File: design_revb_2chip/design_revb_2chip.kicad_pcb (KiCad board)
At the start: 4 copper layers, 0 parts

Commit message: PCB Created
Footprints all placed in the PCB document
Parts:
- added C1: 0.1uF, Capacitor_SMD:C_0201_0603Metric, F.Cu at (72.2, 53.8)
- added C10: 0.1uF, Capacitor_SMD:C_0201_0603Metric, F.Cu at (74.6, 57.2)
- added C11: 0.1uF, Capacitor_SMD:C_0201_0603Metric, F.Cu at (74.6, 59.0)
- added C12: 0.1uF, Capacitor_SMD:C_0201_0603Metric, F.Cu at (74.6, 60.8)
- added C13: 22uF, Capacitor_SMD:C_0201_0603Metric, F.Cu at (74.6, 62.5)
- added C14: 0.1uF, Capacitor_SMD:C_0201_0603Metric, F.Cu at (74.6, 64.2)
- added C15: 0.1uF, Capacitor_SMD:C_0201_0603Metric, F.Cu at (77.1, 53.8)
- added C16: 10uF, Capacitor_SMD:C_0201_0603Metric, F.Cu at (77.1, 55.5)
- added C17: 0.1uF, Capacitor_SMD:C_0201_0603Metric, F.Cu at (77.1, 57.2)
- added C18: 4.7uF, Capacitor_SMD:C_0201_0603Metric, F.Cu at (77.1, 59.0)
- added C19: 0.1uF, Capacitor_SMD:C_0201_0603Metric, F.Cu at (77.1, 60.8)
- added C2: 0.1uF, Capacitor_SMD:C_0201_0603Metric, F.Cu at (72.2, 55.5)
- added C20: 1uF, Capacitor_SMD:C_0201_0603Metric, F.Cu at (77.1, 62.5)
- added C21: 22uF, Capacitor_SMD:C_0201_0603Metric, F.Cu at (77.1, 64.2)
- added C22: 0.1uF, Capacitor_SMD:C_0201_0603Metric, F.Cu at (79.5, 53.8)
- added C23: 0.1uF, Capacitor_SMD:C_0201_0603Metric, F.Cu at (79.5, 55.5)
- added C24: 16pf, Capacitor_SMD:C_0201_0603Metric, F.Cu at (79.5, 57.2)
- added C25: 0.1uF, Capacitor_SMD:C_0201_0603Metric, F.Cu at (79.5, 59.0)
- added C26: 16pf, Capacitor_SMD:C_0201_0603Metric, F.Cu at (79.5, 60.8)
- added C27: 0.1uF, Capacitor_SMD:C_0201_0603Metric, F.Cu at (91.3, 86.5)
- added C28: 0.1uF, Capacitor_SMD:C_0201_0603Metric, F.Cu at (91.3, 88.2)
- added C29: 4.7nF, Capacitor_SMD:C_0201_0603Metric, F.Cu at (91.3, 90.0)
- added C3: 1uF, Capacitor_SMD:C_0201_0603Metric, F.Cu at (72.2, 57.2)
- added C30: 1uF, Capacitor_SMD:C_0201_0603Metric, F.Cu at (91.3, 91.8)
- added C31: 1uF, Capacitor_SMD:C_0201_0603Metric, F.Cu at (91.3, 93.5)
- added C32: 1uF, Capacitor_SMD:C_0201_0603Metric, F.Cu at (91.3, 95.2)
- added C33: 10uF, Capacitor_SMD:C_0201_0603Metric, F.Cu at (93.8, 86.5)
- added C34: 1uF, Capacitor_SMD:C_0201_0603Metric, F.Cu at (93.8, 88.2)
- added C35: 2.2uF, Capacitor_SMD:C_0201_0603Metric, F.Cu at (93.8, 90.0)
- added C36: 100nF, Capacitor_SMD:C_0201_0603Metric, F.Cu at (93.8, 91.8)
- added C37: 2.2uF, Capacitor_SMD:C_0201_0603Metric, F.Cu at (93.8, 93.5)
- added C38: 2.2uF, Capacitor_SMD:C_0201_0603Metric, F.Cu at (93.8, 95.2)
- added C39: 2.2uF, Capacitor_SMD:C_0201_0603Metric, F.Cu at (96.2, 86.5)
- added C4: 0.1uF, Capacitor_SMD:C_0201_0603Metric, F.Cu at (72.2, 59.0)
- added C40: 100nF, Capacitor_SMD:C_0201_0603Metric, F.Cu at (96.2, 88.2)
- added C41: 100nF, Capacitor_SMD:C_0201_0603Metric, F.Cu at (96.2, 90.0)
- added C42: 100nF, Capacitor_SMD:C_0201_0603Metric, F.Cu at (96.2, 91.8)
- added C43: 100nF, Capacitor_SMD:C_0201_0603Metric, F.Cu at (96.2, 93.5)
- added C44: 10nF, Capacitor_SMD:C_0201_0603Metric, F.Cu at (96.2, 95.2)
- added C45: 10nF, Capacitor_SMD:C_0201_0603Metric, F.Cu at (98.7, 86.5)
- added C46: 10nF, Capacitor_SMD:C_0201_0603Metric, F.Cu at (98.7, 88.2)
- added C47: 10nF, Capacitor_SMD:C_0201_0603Metric, F.Cu at (98.7, 90.0)
- added C48: 10nF, Capacitor_SMD:C_0201_0603Metric, F.Cu at (98.7, 91.8)
- added C49: 10uF, Capacitor_SMD:C_0201_0603Metric, F.Cu at (98.7, 93.5)
- added C5: 0.1uF, Capacitor_SMD:C_0201_0603Metric, F.Cu at (72.2, 60.8)
- added C6: 1uF, Capacitor_SMD:C_0201_0603Metric, F.Cu at (72.2, 62.5)
- added C7: 0.1uF, Capacitor_SMD:C_0201_0603Metric, F.Cu at (72.2, 64.2)
- added C8: 0.1uF, Capacitor_SMD:C_0201_0603Metric, F.Cu at (74.6, 53.8)
- added C9: 0.1uF, Capacitor_SMD:C_0201_0603Metric, F.Cu at (74.6, 55.5)
- added D1: GREEN, LED_SMD:LED_0603_1608Metric, F.Cu at (95.7, 62.5)
- added D2: GREEN, LED_SMD:LED_0603_1608Metric, F.Cu at (95.7, 65.1)
- added D3: LED, LED_SMD:LED_0603_1608Metric, F.Cu at (81.5, 90.9)
- added D4: LED, LED_SMD:LED_0603_1608Metric, F.Cu at (81.5, 93.5)
- added D5: LED, LED_SMD:LED_0603_1608Metric, F.Cu at (81.5, 96.0)
- added FB1: FerriteBead, Capstone_Footprints:BEADC1608X95N, F.Cu at (99.7, 62.4)
- added FB2: FerriteBead, Capstone_Footprints:BEADC1608X95N, F.Cu at (99.7, 65.0)
- added J1: USB_C_Receptacle, Connector_USB:USB_C_Receptacle_Amphenol_12401610E4-2A_CircularHoles, F.Cu at (159.3, 72.5)
- added J2: Conn_01x08, Connector_PinHeader_2.00mm:PinHeader_1x08_P2.00mm_Horizontal, F.Cu at (170.0, 93.0)
- added J3: 09452812810, Capstone_Footprints:09452812810, F.Cu at (246.3, 72.2)
- added JP1: Jumper_2_Bridged, Jumper:SolderJumper-2_P1.3mm_Bridged_Pad1.0x1.5mm, F.Cu at (99.8, 72.7)
- added JP2: Jumper_2_Open, Jumper:SolderJumper-3_P1.3mm_Open_Pad1.0x1.5mm, F.Cu at (87.3, 87.4)
- added JP3: Jumper_2_Open, Jumper:SolderJumper-3_P1.3mm_Open_Pad1.0x1.5mm, F.Cu at (87.3, 91.2)
- added JP4: Jumper_2_Open, Jumper:SolderJumper-3_P1.3mm_Open_Pad1.0x1.5mm, F.Cu at (87.3, 95.1)
- added JP5: Jumper_2_Bridged, Jumper:SolderJumper-2_P1.3mm_Bridged_Pad1.0x1.5mm, F.Cu at (99.8, 76.2)
- added L1: 3.3uH, Inductor_SMD_Wurth:L_Wurth_WE-LQSH-3012, F.Cu at (88.2, 64.5)
- added L2: 2.2uH, Inductor_SMD:L_1008_2520Metric, F.Cu at (67.9, 81.0)
- added R1: 1k, Resistor_SMD:R_0805_2012Metric, F.Cu at (83.4, 36.3)
- added R10: 10k, Resistor_SMD:R_0805_2012Metric, F.Cu at (87.8, 42.2)
- added R11: 470k, Resistor_SMD:R_0805_2012Metric, F.Cu at (87.8, 45.1)
- added R12: 150k, Resistor_SMD:R_0805_2012Metric, F.Cu at (87.8, 48.1)
- added R13: 10k, Resistor_SMD:R_0805_2012Metric, F.Cu at (92.2, 36.3)
- added R14: 10k, Resistor_SMD:R_0805_2012Metric, F.Cu at (92.2, 39.2)
- added R15: 330R, Resistor_SMD:R_0805_2012Metric, F.Cu at (92.2, 42.2)
- added R16: 10k, Resistor_SMD:R_0805_2012Metric, F.Cu at (86.6, 72.3)
- added R17: 1k, Resistor_SMD:R_0805_2012Metric, F.Cu at (86.6, 75.3)
- added R18: 1k, Resistor_SMD:R_0805_2012Metric, F.Cu at (86.6, 78.2)
- added R19: 100k, Resistor_SMD:R_0805_2012Metric, F.Cu at (86.6, 81.2)
- added R2: 10k, Resistor_SMD:R_0805_2012Metric, F.Cu at (83.4, 39.2)
- added R20: 2.2k, Resistor_SMD:R_0805_2012Metric, F.Cu at (86.6, 84.2)
- added R21: 2.49k, Resistor_SMD:R_0805_2012Metric, F.Cu at (91.0, 72.3)
- added R22: 470, Resistor_SMD:R_0805_2012Metric, F.Cu at (91.0, 75.3)
- added R23: 470, Resistor_SMD:R_0805_2012Metric, F.Cu at (91.0, 78.2)
- added R24: 2.49k, Resistor_SMD:R_0805_2012Metric, F.Cu at (91.0, 81.2)
- added R25: 470, Resistor_SMD:R_0805_2012Metric, F.Cu at (91.0, 84.2)
- added R26: 2.49k, Resistor_SMD:R_0805_2012Metric, F.Cu at (95.5, 72.3)
- added R27: 2.49k, Resistor_SMD:R_0805_2012Metric, F.Cu at (95.5, 75.3)
- added R28: 2.49k, Resistor_SMD:R_0805_2012Metric, F.Cu at (95.5, 78.2)
- added R29: 2.49k, Resistor_SMD:R_0805_2012Metric, F.Cu at (95.5, 81.2)
- added R3: 10k, Resistor_SMD:R_0805_2012Metric, F.Cu at (83.4, 42.2)
- added R4: 1k, Resistor_SMD:R_0805_2012Metric, F.Cu at (83.4, 45.1)
- added R5: 10k, Resistor_SMD:R_0805_2012Metric, F.Cu at (83.4, 48.1)
- added R6: 12k, Resistor_SMD:R_0402_1005Metric, F.Cu at (103.1, 62.2)
- added R7: 10k, Resistor_SMD:R_0805_2012Metric, F.Cu at (87.8, 36.3)
- added R8: 2k, Resistor_SMD:R_0402_1005Metric, F.Cu at (103.1, 64.2)
- added R9: 100k, Resistor_SMD:R_0805_2012Metric, F.Cu at (87.8, 39.2)
- added U1: LAN7801-I/9JX, Capstone_Footprints:SQFN64_9JX_MCH, F.Cu at (189.8, 73.6)
- added U2: TPS62162QDSGRQ1, Capstone_Footprints:DSG0008A, F.Cu at (192.5, 88.3)
- added U3: 93C56A-I/P, Capstone_Footprints:PDIP8_300MC_MCH, F.Cu at (175.9, 54.4)
- added U4: DP83TG720SWRHARQ1, Capstone_Footprints:VQFN36_6X6_TEX, F.Cu at (216.0, 73.6)
- added U5: TPS784105QWDRBRQ1, Capstone_Footprints:DRB0008J-IPC_A, F.Cu at (241.0, 69.5)
- added XTAL1: ECS-250-18-36B2-CTY-TR, Capstone_Footprints:ECX-2236B2_ECS, F.Cu at (179.0, 94.9)

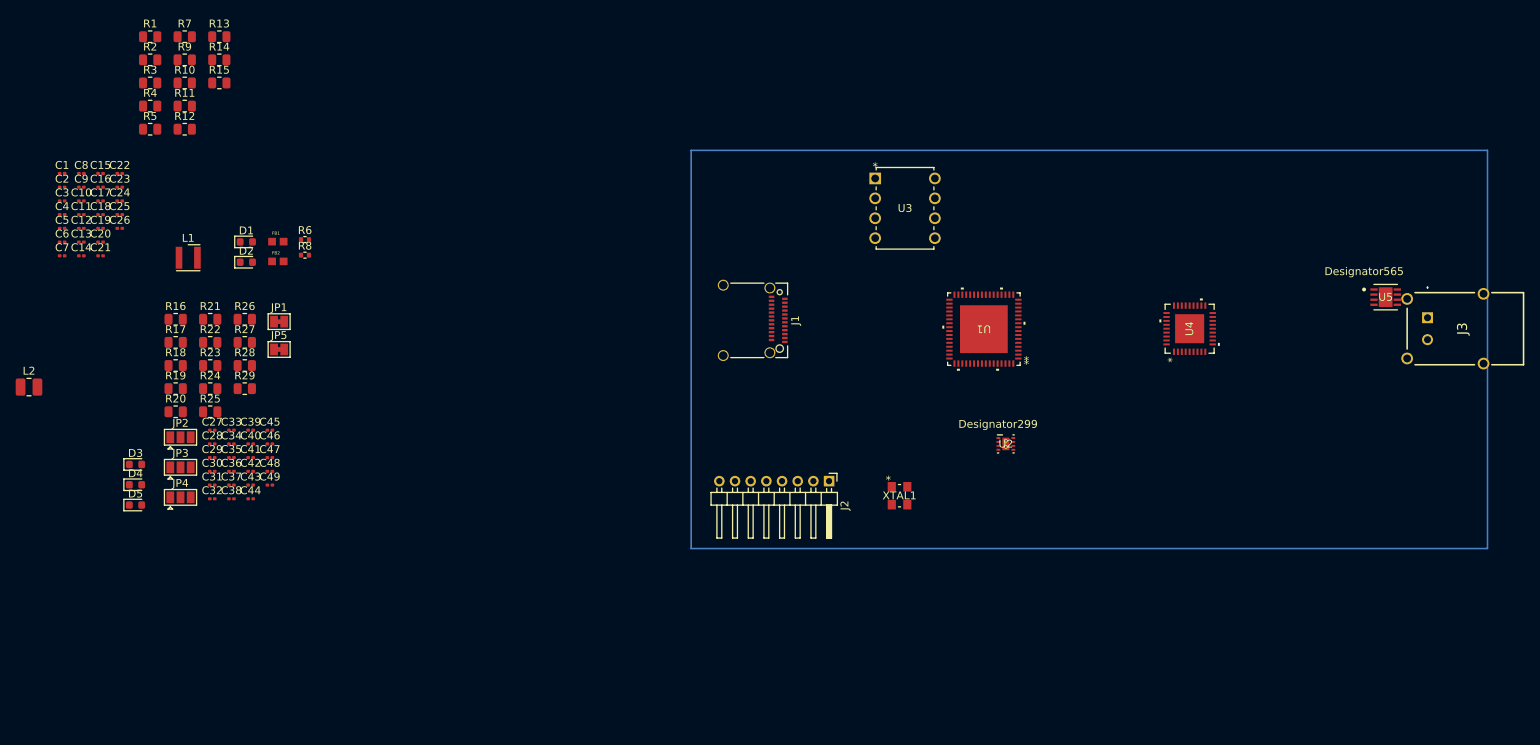
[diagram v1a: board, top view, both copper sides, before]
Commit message: Some PCB Design
- USB side PCB design (mostly done)
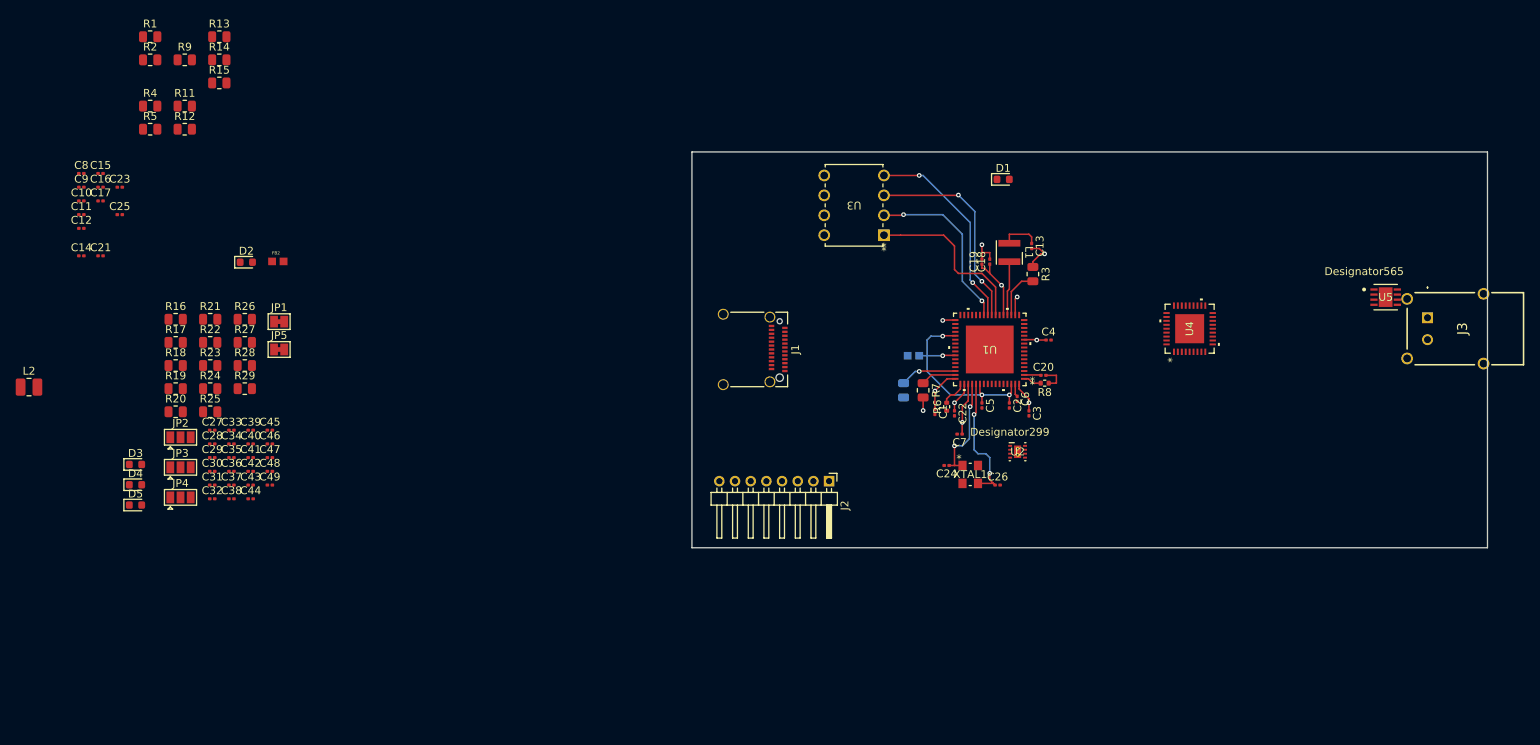
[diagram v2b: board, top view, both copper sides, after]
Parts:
- FB1, R10: moved to B.Cu
- moved C4 126.9 mm to (198.0, 75.0)
- moved C3 126.3 mm to (195.5, 84.3), turned to -90 degrees
- moved C2 124.0 mm to (193.0, 83.3), turned to -90 degrees
- moved C6 123.5 mm to (194.0, 82.5), turned to -90 degrees
- moved C20 121.5 mm to (197.3, 79.5)
- moved C13 121.2 mm to (195.8, 63.0), turned to -90 degrees
- moved C5 119.5 mm to (189.5, 83.3), turned to -90 degrees
- moved C7 116.7 mm to (186.7, 87.0), turned to 180 degrees
- moved C26 116.7 mm to (191.5, 93.5)
- moved C1 115.4 mm to (183.5, 84.2), turned to -90 degrees
- moved R3 115.2 mm to (196.0, 66.6), turned to -90 degrees
- moved C18 113.6 mm to (190.5, 65.0), turned to 90 degrees
- moved C19 112.5 mm to (189.5, 65.0), turned to 90 degrees
- moved C22 110.8 mm to (186.0, 84.3), turned to -90 degrees
- moved C24 110.8 mm to (185.0, 91.0), turned to 180 degrees
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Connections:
- C23 pad 1: VPP -> VDD33A
- U1 pad 33: VPP -> VDD33A
- U3 pad 8: VPP -> VDD33A
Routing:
- net VDD33A: track 0.00 -> 63.6 mm, vias 0 -> 9
- net VDD12A: track 0.00 -> 29.3 mm, vias 0 -> 4
- net Net-(U1-EEDI/GPIO1): track 0.00 -> 26.6 mm, vias 0 -> 2
- net Net-(U1-EEDO/GPIO2): track 0.00 -> 26.2 mm, vias 0 -> 2
- net Net-(U1-EECLK/GPIO3): track 0.00 -> 22.5 mm, vias 0 -> 2
- net Net-(U1-EECS/GPIO0): track 0.00 -> 22.3 mm
- net XO: track 0.00 -> 17.0 mm, vias 0 -> 2
- net GND: track 0.00 -> 13.9 mm, vias 0 -> 2
- net XI: track 0.00 -> 13.6 mm, vias 0 -> 2
- net TEST: track 0.00 -> 7.25 mm, vias 0 -> 1
- net VDD12_SW_OUT: track 0.00 -> 6.91 mm
- net Net-(U1-CLK125): track 0.00 -> 6.29 mm
- net VDD12: track 0.00 -> 4.97 mm
- net RESET_N: track 0.00 -> 4.54 mm
- net USBRBIAS: track 0.00 -> 3.42 mm
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- added copper zone on In1.Cu, net 3.3V
- added copper zone on In2.Cu, net 3.3V
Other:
- board outline added: 101.5 x 50.5 mm

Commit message: More PCB 2
- USB side PCB Update
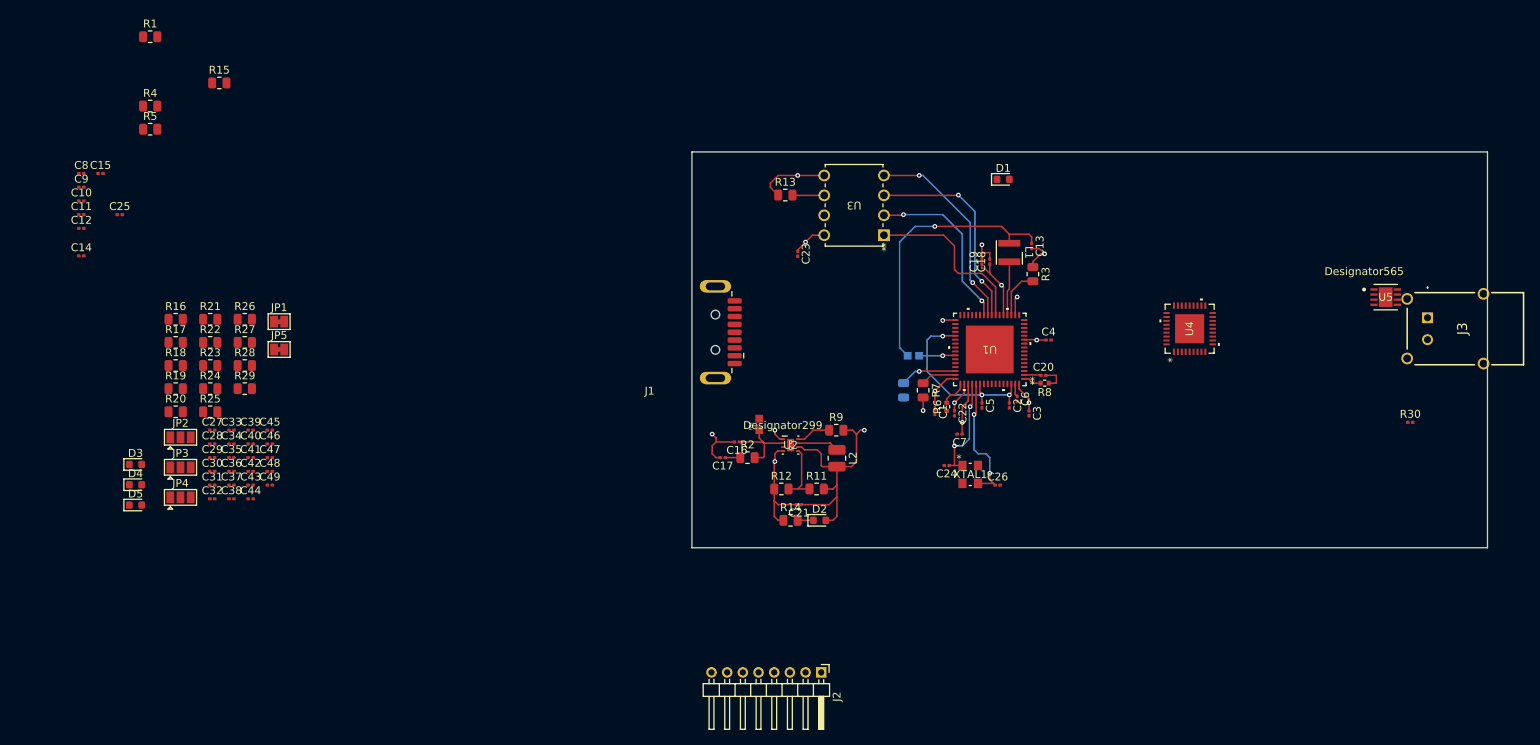
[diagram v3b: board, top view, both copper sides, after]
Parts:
- added R30: 330R, Capacitor_SMD:C_0201_0603Metric, F.Cu at (244.2, 85.5)
- J1: footprint Connector_USB:USB_C_Receptacle_Amphenol_12401610E4-2A_CircularHoles -> Connector_USB:USB3_A_Plug_Wuerth_692112030100_Horizontal
- R17, R18: value 1k -> 1k 1%
- R19: value 100k -> 100k 1%
- moved L2 103.5 mm to (171.0, 90.1), turned to -90 degrees
- moved R9 95.6 mm to (170.9, 86.5)
- moved C21 94.6 mm to (166.2, 96.0), turned to 180 degrees
- moved R11 94.3 mm to (168.4, 94.0)
- moved R14 93.6 mm to (165.1, 98.0)
- moved R2 91.6 mm to (159.6, 90.0)
- moved R12 88.9 mm to (163.9, 94.0)
- moved C16 87.5 mm to (158.2, 88.0), turned to 180 degrees
- moved C23 86.9 mm to (166.0, 64.0), turned to -90 degrees
- moved C17 85.9 mm to (156.4, 90.0), turned to 180 degrees
- moved D2 80.2 mm to (168.8, 98.0)
- moved R13 75.0 mm to (164.4, 56.5)
- moved FB2 64.8 mm to (161.1, 85.8), turned to 90 degrees
- moved U2 29.0 mm to (165.1, 88.4)
- moved J2 24.4 mm to (169.0, 117.4)
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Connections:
- net /ETH_SIDE/Vdd renamed Vdd
- C28 pad 1: Net-(J3-BI_DA-) -> Net-(J3-BI_DA+)
- J3 pad 2: Net-(J3-BI_DA-) -> Net-(J3-BI_DA+)
- J3 pad 3: GND -> Net-(J3-GND_1)
- J3 pad 4: GND -> Net-(J3-GND_1)
- J3 pad 5: GND -> Net-(J3-GND_1)
- J3 pad 6: GND -> Net-(J3-GND_1)
- R18 pad 1: Net-(J3-BI_DA-) -> Net-(J3-BI_DA+)
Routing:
- net GND: track 13.9 -> 50.0 mm, vias 2 -> 6
- net 3.3V: track 0.00 -> 33.5 mm, vias 0 -> 1
- net VDD12: track 4.97 -> 35.1 mm, vias 0 -> 1
- net 5V: track 0.00 -> 10.6 mm
- net Net-(U2-FB): track 0.00 -> 7.99 mm
- net VDD33A: track 63.6 -> 69.2 mm, vias 9 -> 10
- net Net-(U2-SW): track 0.00 -> 5.31 mm
- net Net-(U2-PG): track 0.00 -> 4.44 mm
- net Net-(U3-ORG): track 0.00 -> 4.07 mm
- net Net-(D2-K): track 0.00 -> 2.00 mm
- net Net-(U2-EN): track 0.00 -> 1.92 mm

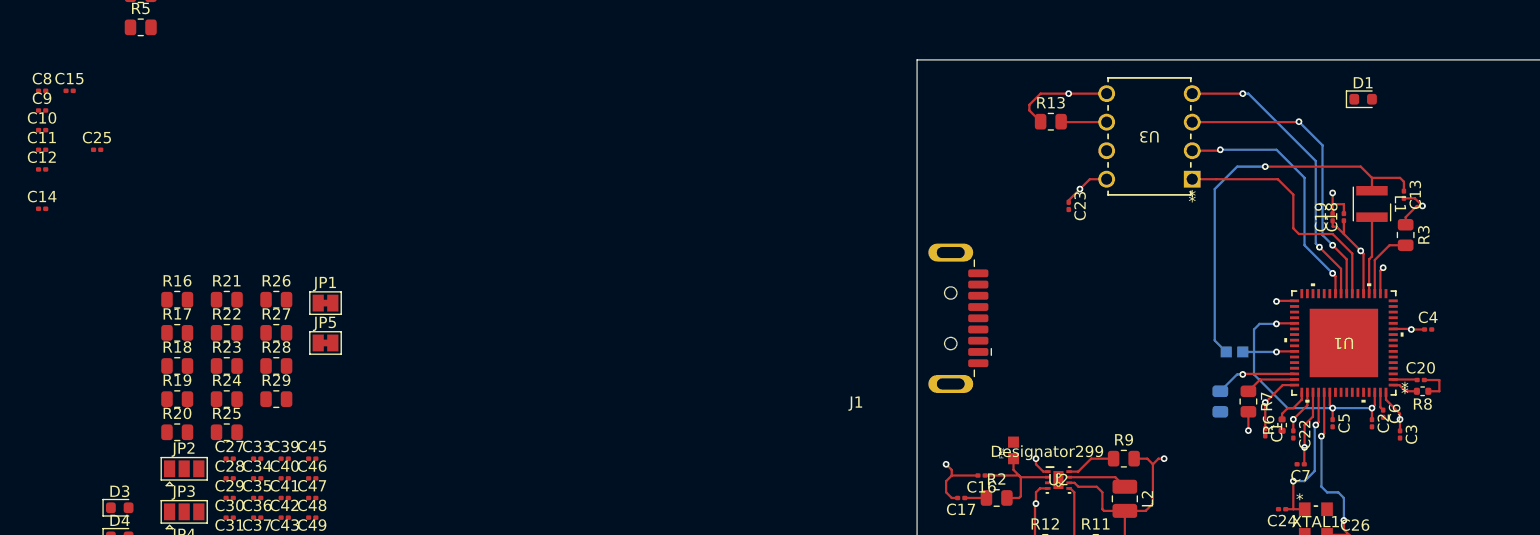
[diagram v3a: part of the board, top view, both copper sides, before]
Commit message: USB Side PCB Update
- small update to the PCB on the USB side
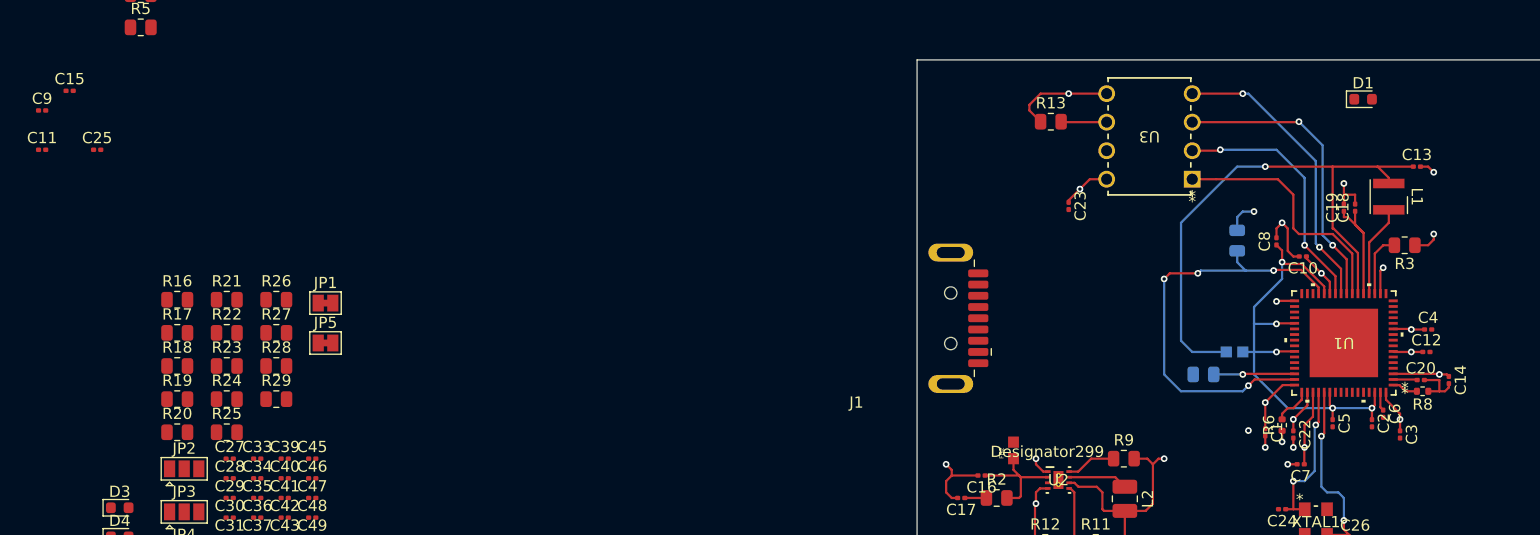
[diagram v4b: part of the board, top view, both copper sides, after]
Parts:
- R7: moved to B.Cu
- moved C14 126.2 mm to (199.8, 79.5), turned to -90 degrees
- moved C12 124.3 mm to (197.8, 77.0)
- moved C10 112.8 mm to (186.8, 68.5), turned to 180 degrees
- moved C8 110.7 mm to (184.5, 67.2), turned to 90 degrees
- moved R7 14.4 mm to (181.0, 67.1), turned to 90 degrees
- moved R10 2.84 mm to (178.0, 79.0), turned to 0 degrees
- moved C13 2.75 mm to (197.0, 60.5), turned to 0 degrees
- moved L1 1.63 mm to (194.5, 63.2)
- moved C18 1.31 mm to (191.5, 64.2)
- moved C19 1.31 mm to (190.5, 64.2)
- moved R3 0.92 mm to (195.9, 67.5), turned to 180 degrees
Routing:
- net RESET_N: track 4.54 -> 38.6 mm, vias 0 -> 4
- net VDD33A: track 69.2 -> 100.9 mm, vias 10 -> 13
- net GND: track 50.0 -> 66.7 mm, vias 6 -> 12
- net VDD12: track 35.1 -> 51.9 mm
- net VDD12A: track 29.3 -> 43.1 mm, vias 4 -> 5
- net VDD12_SW_OUT: track 6.91 -> 8.18 mm
- net Net-(U1-CLK125): track 6.29 -> 5.62 mm

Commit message: PCB Update
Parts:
- J1: footprint Connector_USB:USB3_A_Plug_Wuerth_692112030100_Horizontal -> Connector_USB:USB_C_Receptacle_Molex_105450-0101
- moved R4 89.4 mm to (170.6, 65.0)
- moved C25 80.4 mm to (156.0, 83.8), turned to -90 degrees
- moved R15 78.3 mm to (158.5, 83.9), turned to 90 degrees
- moved J2 28.7 mm to (190.0, 97.9)
- moved D1 20.8 mm to (174.2, 65.0), turned to 180 degrees
- moved J1 9.96 mm to (157.1, 74.4), turned to -90 degrees
- moved C13 4.00 mm to (197.0, 56.5)
- moved C18 4.00 mm to (191.5, 60.2)
- moved C19 4.00 mm to (190.5, 60.2)
- moved L1 4.00 mm to (194.5, 59.2)
- moved R3 4.00 mm to (195.9, 63.5)
- moved C10 1.89 mm to (188.3, 67.3)
- moved C8 1.89 mm to (186.0, 66.0)
- moved R13 1.68 mm to (166.1, 56.5)
- moved R7 1.50 mm to (179.5, 67.1)
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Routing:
- net GND: track 66.7 -> 105.2 mm, vias 12 -> 23
- net USB_SHIELD: track 0.00 -> 36.9 mm, vias 0 -> 2
- net VBUS: track 0.00 -> 17.1 mm, vias 0 -> 3
- net Net-(D1-K): track 0.00 -> 16.5 mm
- net VDD33A: track 100.9 -> 111.5 mm, vias 13 -> 14
- net VDD12: track 51.9 -> 57.9 mm
- net Net-(U1-CLK125): track 5.62 -> 9.62 mm
- net VDD12_SW_OUT: track 8.18 -> 12.2 mm
- net RESET_N: track 38.6 -> 42.1 mm
- net VDD12A: track 43.1 -> 45.4 mm
- net Net-(D1-A): track 0.00 -> 1.93 mm
- net Net-(U3-ORG): track 4.07 -> 2.40 mm
- net Net-(U1-EECLK/GPIO3): track 22.5 -> 23.7 mm
- net TEST: track 7.21 -> 6.13 mm
- net Net-(U1-EEDI/GPIO1): track 26.6 -> 27.2 mm
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- added copper zone on In1.Cu, net GND
- removed copper zone on In1.Cu, net 3.3V
